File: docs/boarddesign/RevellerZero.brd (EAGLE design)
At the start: 65 x 30 mm, 23 parts, among them IC100 6581, Q100 IRF9Z24N, T100 BC547, X101 PG203J, X102 CANTON-POWER

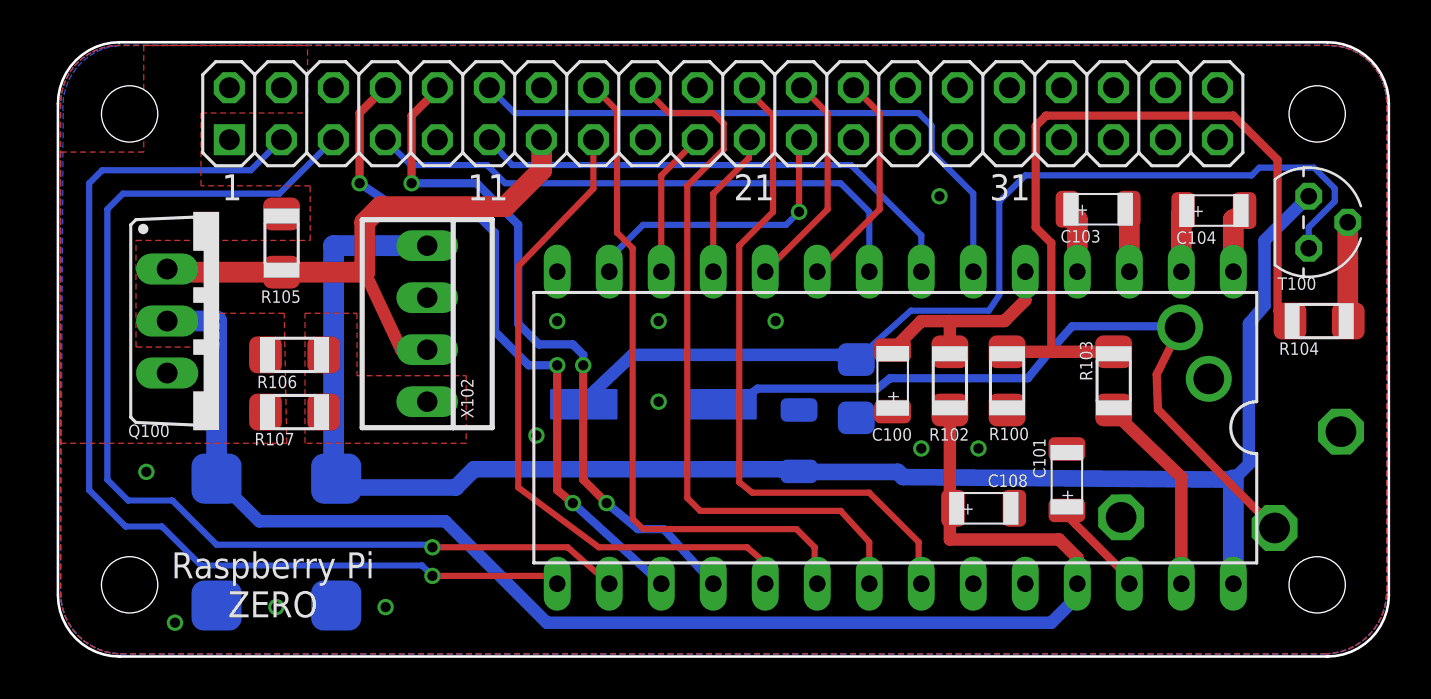
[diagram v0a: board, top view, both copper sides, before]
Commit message: Added box design and revised RevellerZero design
Raspberry Pi Rev B box design to allow for reveller HAT. Can be printed
with or without vented design. Designed in Solidworks 2016. RevellerZero
board design was revised due to CantonPower being placed slightly off
board.
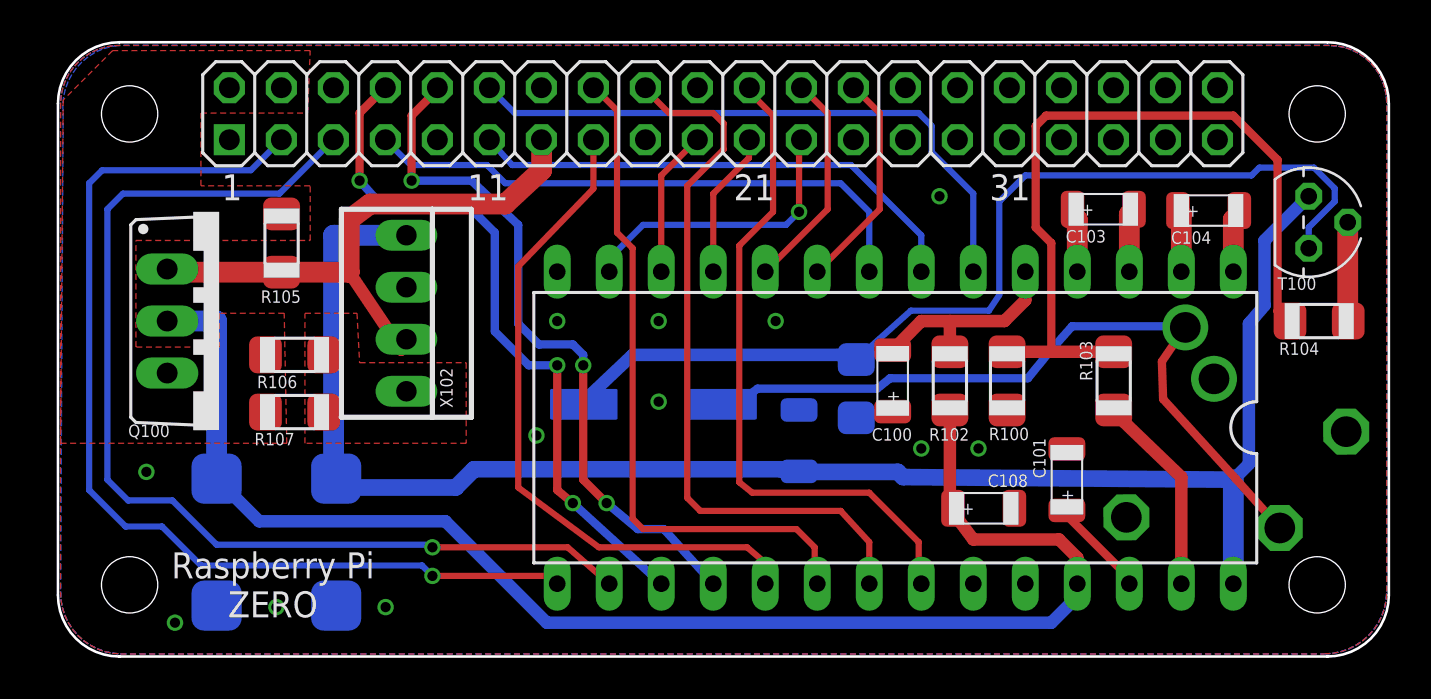
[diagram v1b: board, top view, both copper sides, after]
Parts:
- moved X102 1.14 mm to (17.0, 16.8)
- moved C103 0.25 mm to (51.1, 21.8)
- moved C104 0.25 mm to (56.2, 21.8)
- moved X101 0.25 mm to (57.9, 11.2)
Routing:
- net +5V_SID: track 70.6 -> 69.8 mm
- net +12V: track 81.0 -> 80.5 mm

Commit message: Revision of RevellerZero boarddesign
Moved Cantonpower closer to gpio pins and a little further away from sid
chip as its currently hitting the chip.
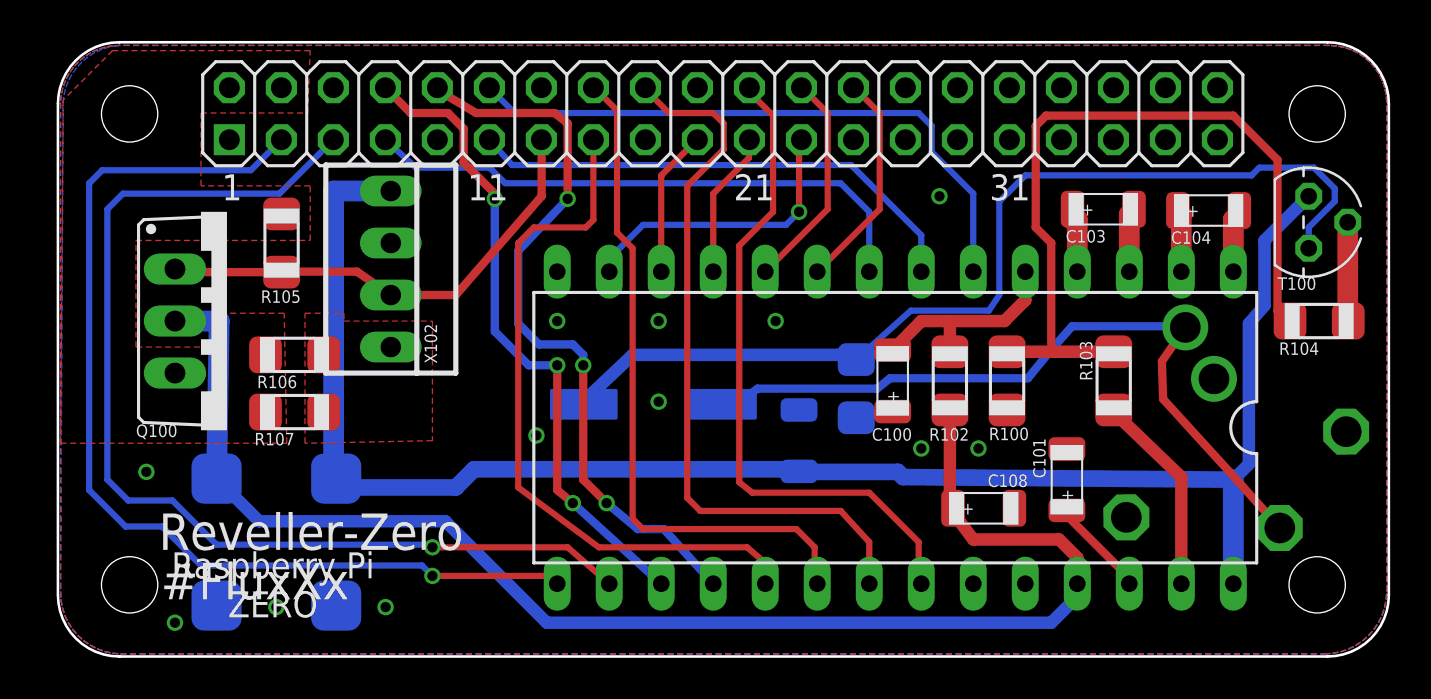
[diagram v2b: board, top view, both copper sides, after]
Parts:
- moved X102 2.29 mm to (16.3, 18.9)
- moved Q100 0.38 mm to (8.26, 16.4)
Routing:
- net PWCTL: track 28.4 -> 23.3 mm
- net D2: track 34.3 -> 31.9 mm
- net D3: track 34.3 -> 36.1 mm
- net D4: track 32.8 -> 34.3 mm
- net +12V: track 80.5 -> 81.9 mm
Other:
- board text added: "#FluxXx"
- board text added: "Reveller-Zero"
